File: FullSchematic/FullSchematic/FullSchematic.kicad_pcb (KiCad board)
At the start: 2 copper layers, 58 parts, among them IC1 TTP223E-BA6, J1 USB_B_Micro, J2 TP4056, Q1 PMOS, U1 LM1117-3.3, U2 CH340C, U3 24LC64

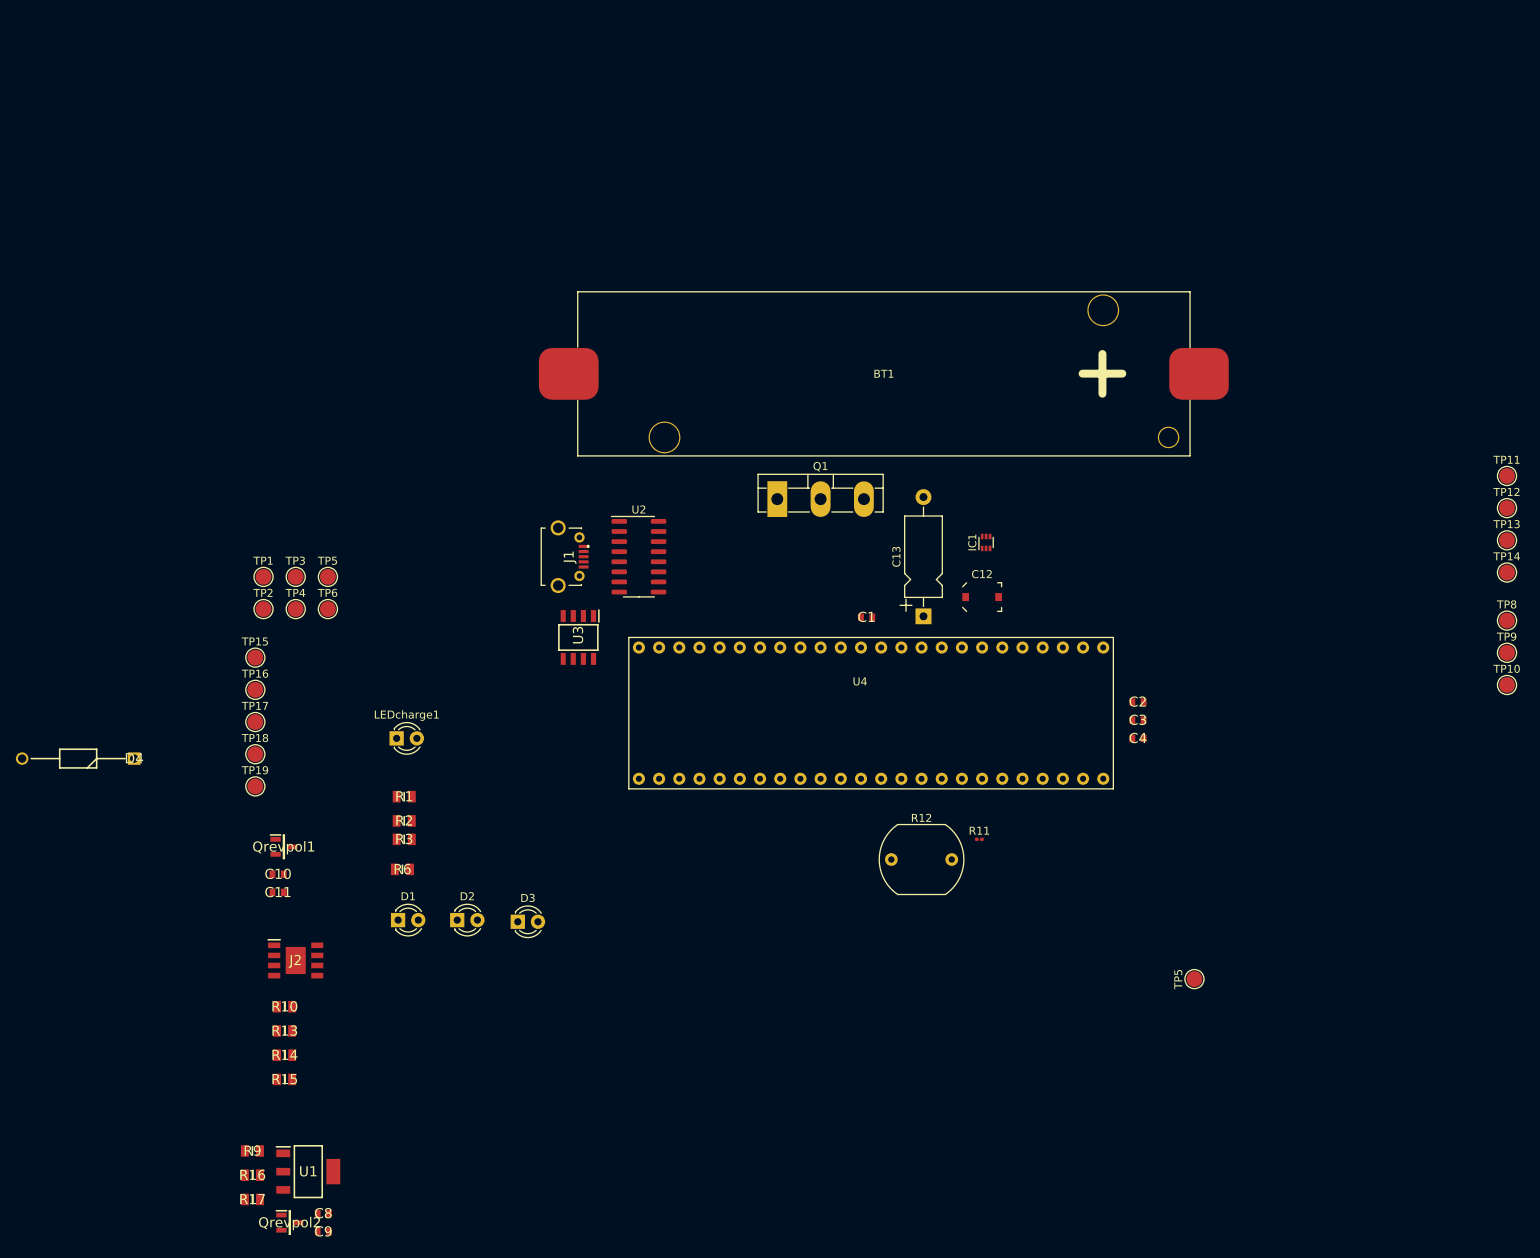
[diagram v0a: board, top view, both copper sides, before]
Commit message: connected sensors adnd created touch pad
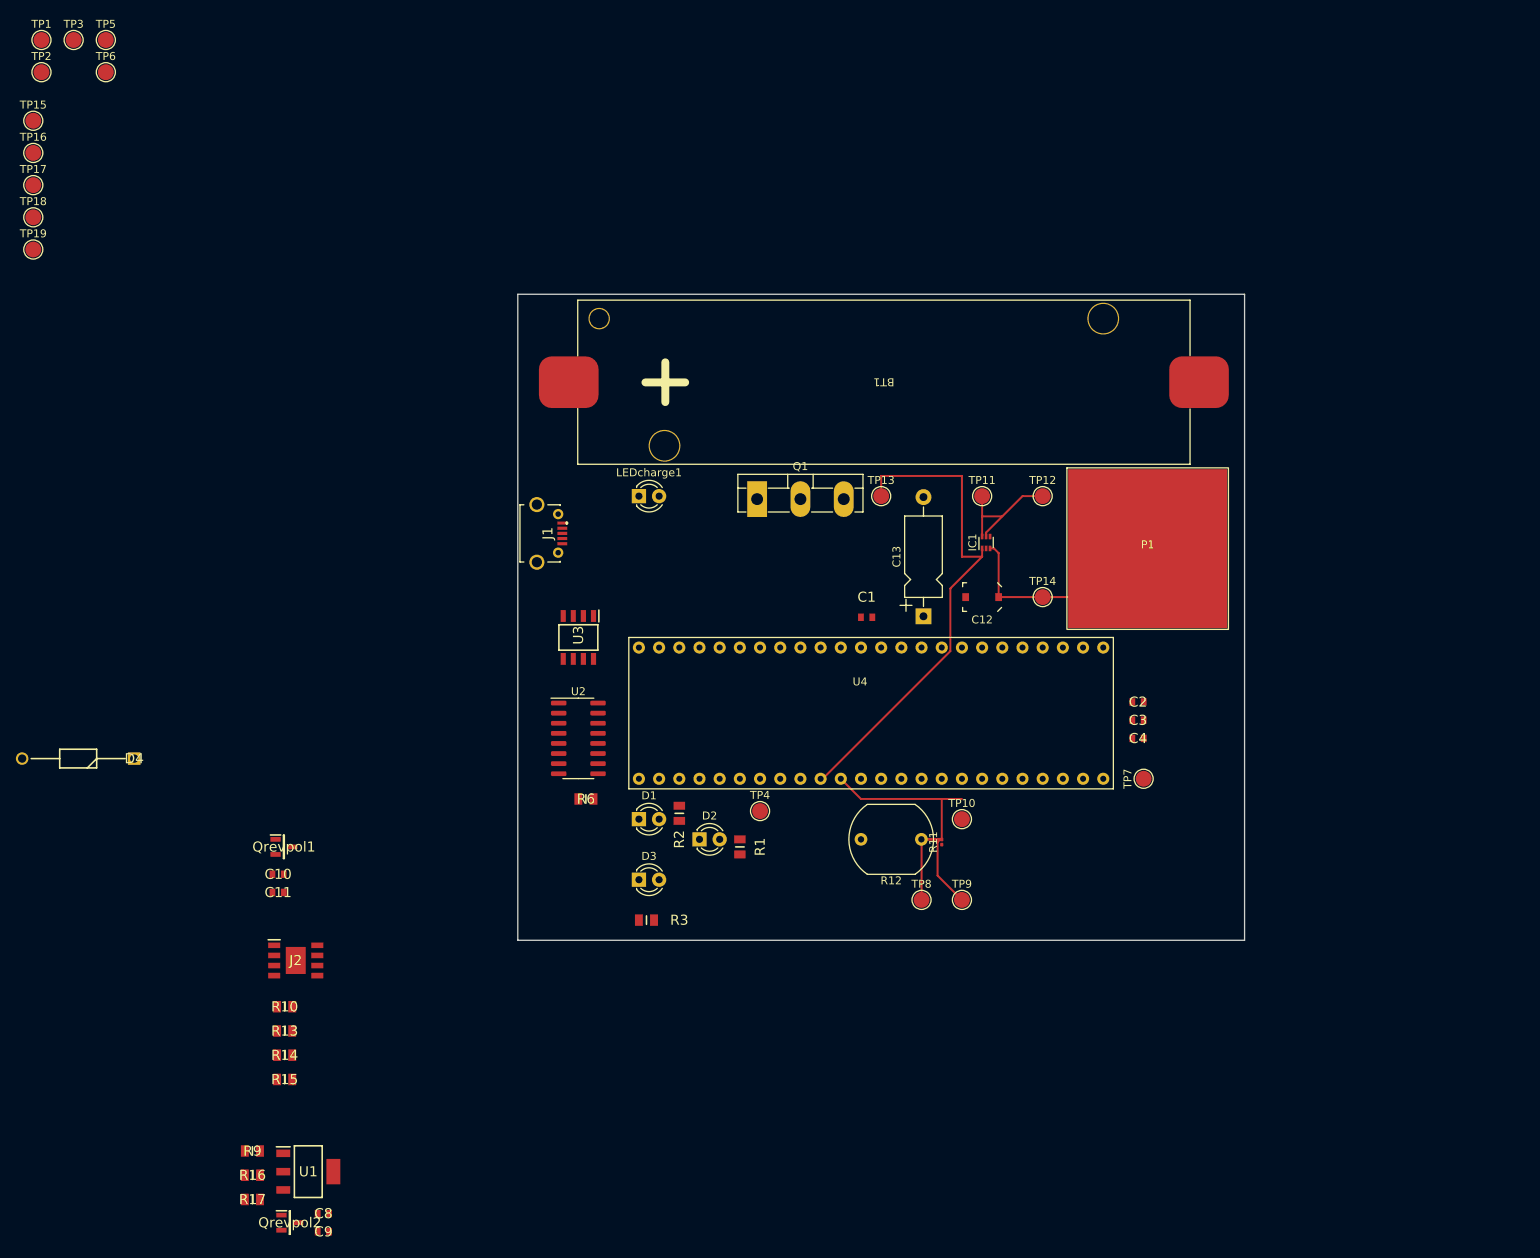
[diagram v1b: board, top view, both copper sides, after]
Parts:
- added P1: ~, Library:Touch Pad, F.Cu at (160.5, 82.8)
- moved TP8 81.6 mm to (132.1, 127.0)
- moved TP13 78.9 mm to (127.0, 76.2)
- moved TP9 75.3 mm to (137.2, 127.0)
- moved TP17 73.1 mm to (20.3, 37.1)
- moved TP18 73.1 mm to (20.3, 41.1)
- moved TP1 73.1 mm to (21.4, 18.8)
- moved TP15 73.1 mm to (20.3, 29.0)
- moved TP19 73.1 mm to (20.3, 45.2)
- moved TP2 73.1 mm to (21.4, 22.9)
- moved TP3 73.1 mm to (25.4, 18.8)
- moved TP5 73.1 mm to (29.4, 18.8)
- moved TP6 73.1 mm to (29.4, 22.9)
- moved TP16 73.1 mm to (20.3, 33.0)
- moved TP10 70.6 mm to (137.2, 116.8)
- moved TP11 66.1 mm to (139.7, 76.2)
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- renumbered TP5 to TP7
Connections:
- net /Sensors/Digital Sensor/Touch Pad renamed Net-(IC1-I)
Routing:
- net /Microcontroller/T_sensor: track 0.00 -> 63.0 mm
- net /Microcontroller/LDR_sensor: track 0.00 -> 40.8 mm
- net Net-(IC1-I): track 0.00 -> 28.1 mm
- net /Power Module/Vboard: track 0.00 -> 17.1 mm
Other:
- board outline added: 91.4 x 81.3 mm

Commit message: connected microcontroller
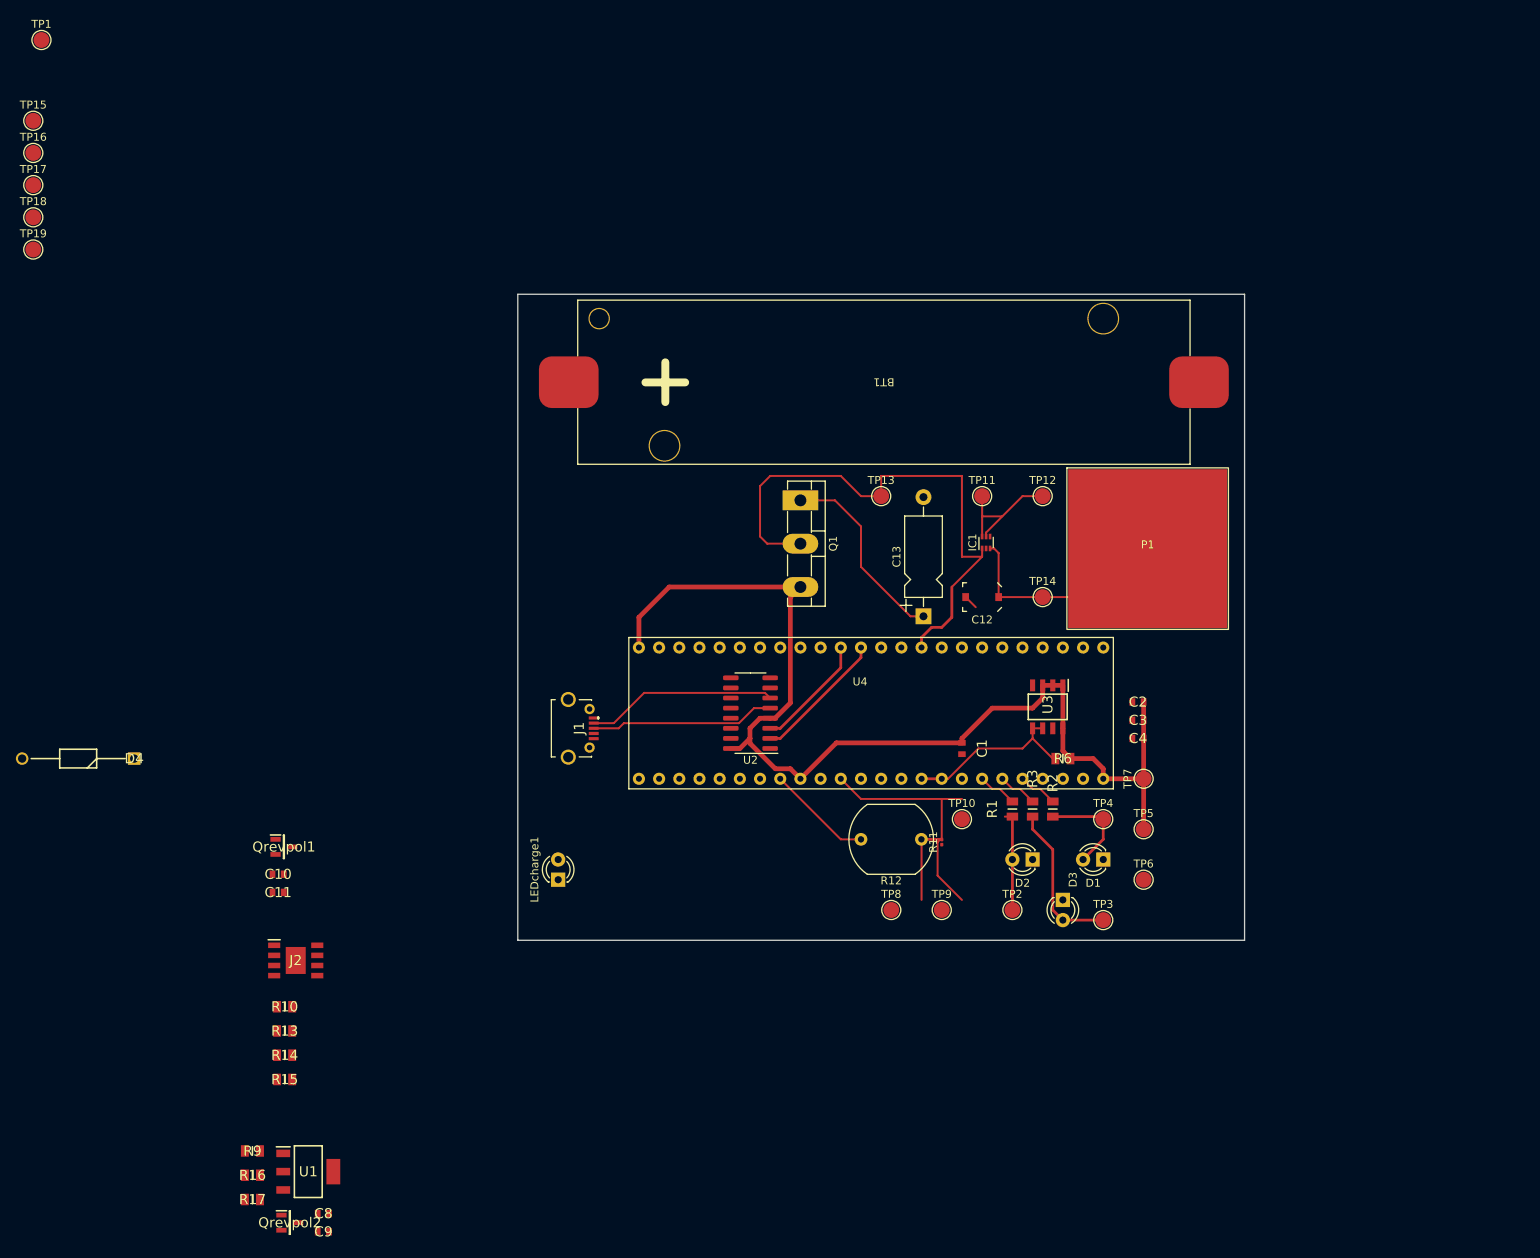
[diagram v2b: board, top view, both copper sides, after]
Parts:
- moved TP3 170.4 mm to (154.9, 129.5)
- moved TP6 165.4 mm to (160.0, 124.5)
- moved TP5 164.0 mm to (160.0, 118.1)
- moved TP2 161.4 mm to (143.5, 128.3)
- moved R6 60.2 mm to (149.9, 109.2), turned to 0 degrees
- moved U3 59.7 mm to (148.0, 102.7)
- moved D1 58.6 mm to (154.9, 121.9), turned to 180 degrees
- moved D3 53.4 mm to (149.9, 127.0), turned to -90 degrees
- moved R3 50.5 mm to (146.1, 115.6), turned to -90 degrees
- moved LEDcharge1 49.3 mm to (86.4, 124.5), turned to 90 degrees
- moved R2 47.0 mm to (148.6, 115.6), turned to -90 degrees
- moved TP4 43.2 mm to (154.9, 116.8)
- moved D2 42.0 mm to (146.1, 121.9), turned to 180 degrees
- moved R1 34.6 mm to (143.5, 115.6), turned to -90 degrees
- moved J1 24.8 mm to (87.6, 105.4)
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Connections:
- P1 pad Touch Pad1: Net-(IC1-I) -> (no net)
- U4 pad 10: /Microcontroller/T_sensor -> unconnected-(U4-PA0-Pad10)
- U4 pad 12: /Microcontroller/PA2 -> unconnected-(U4-PA2-Pad12)
- U4 pad 13: /Microcontroller/PA3 -> unconnected-(U4-PA3-Pad13)
- U4 pad 19: /Microcontroller/out2 -> /Microcontroller/out3
- U4 pad 20: /Microcontroller/out3 -> /Microcontroller/out2
- U4 pad 34: unconnected-(U4-PA13-Pad34) -> /Microcontroller/T_sensor
- U4 pad 37: unconnected-(U4-PA14-Pad37) -> /Microcontroller/PA2
- U4 pad 38: unconnected-(U4-PA15-Pad38) -> /Microcontroller/PA3
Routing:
- net /Microcontroller/3.3V: track 0.00 -> 136.0 mm
- net /Power Module/Vboard: track 17.1 -> 41.6 mm
- net Net-(J1-D-): track 0.00 -> 24.0 mm
- net Net-(J1-D+): track 0.00 -> 23.3 mm
- net /Microcontroller/SCL: track 0.00 -> 22.5 mm
- net Net-(D3-A): track 0.00 -> 19.7 mm
- net /Microcontroller/PA2: track 0.00 -> 16.9 mm
- net GND: track 0.00 -> 15.2 mm
- net /Microcontroller/PA3: track 0.00 -> 14.6 mm
- net Net-(D2-A): track 0.00 -> 12.7 mm
- net Net-(D1-A): track 0.00 -> 12.6 mm
- net /Microcontroller/T_sensor: track 63.0 -> 70.4 mm
- net /Microcontroller/out3: track 0.00 -> 4.99 mm
- net /Microcontroller/out2: track 0.00 -> 4.99 mm
- net /Microcontroller/out1: track 0.00 -> 4.99 mm
